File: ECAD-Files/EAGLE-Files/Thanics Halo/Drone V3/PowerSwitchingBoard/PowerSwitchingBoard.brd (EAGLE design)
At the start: 70 x 50 mm, 72 parts, among them IC1 MEGA8-AI, J1 ESC_CONTACTS, Q1 BC817, Q2 BC817, Q3 IRLR8726, Q4 IRLR8726, Q5 IRLR8726, Q6 IRLR8726, Q7 BC817, Q8 IRLR8726, Q9 IRLR8726, U1 TPS65261RHBR

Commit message: Added Flight ESCs and power supply to PowerSwitchingBoard
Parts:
- removed R12: 10k, 10k-resistor:RC0805N
- added C10, C48, C6: 470uF, 470uF-capacitor:PCAP_10X10-ELECT-M
- added C11, C27, C45: 10nF, thanics_robotics:0603_CAPACITOR
- added C12, C38, C46: 0.1uF, 0.1uF X7R Ceramic Capacitor:0805
- added C26, C44, C47, C9: 10uF, 10uF X5R Ceramic Capacitor:G-21
- added C28, C29, C30, C33, C34, C35, C39, C40, C41: 0.1uF (50V), 0.1uF-capacitor-0402:0402-M
- added C31, C36, C42, C5: 0.1uF, 0.1uF-capacitor-0402:0402-M
- added C32, C37, C43, C7: 2.2uF, 2.2uF X5R Capacitor:G-188-M
- added C8: 22uF, 22uF X5R Ceramic Capacitor:G-21
- added D10, D11, D12, D13, D14, D15, D7, D8, D9: 1N4148, 1n4148w-diode:SOD123-M
- added IC3, IC4, IC5: MEGA8-AI, atmel:TQFP32-08
- added JP3, JP4, JP5: JUMPER-SMT_2_NO_NO-SILK, SparkFun-Jumpers:SMT-JUMPER_2_NO_NO-SILK
- added Q19, Q22, Q25, Q28, Q31, Q34, Q37, Q40, Q43: BC817, SparkFun-DiscreteSemi:SOT23-3
- added Q20, Q21, Q23, Q24, Q26, Q27, Q29, Q30, Q32, Q33, Q35, Q36, Q38, Q39, Q41, Q42, Q44, Q45: IRLR8726, thanics_robotics:DPAK
- added R100, R105, R121, R127, R132, R67, R73, R78, R94: 2.2k, 2.2k-resistor:RC0603N-M
- added R101, R106, R114, R115, R116, R122, R128, R133, R141, R142, R143, R68, R74, R79, R87, R88, R89, R95: 4.7k, 4.7k-resistor:RC0603N-M
- added R102, R103, R107, R108, R124, R125, R129, R130, R134, R135, R70, R71, R75, R76, R80, R81, R97, R98: 100R, 100-resistor:RC0603N-M
- added R104, R117, R118, R119, R120, R126, R131, R144, R145, R37, R38, R65, R66, R72, R77, R90, R91, R92, R93, R99: 10k, 10k-resistor(0603):RC0603N-M
- added R109, R110, R111, R112, R113, R123, R136, R137, R138, R139, R140, R69, R82, R83, R84, R85, R86, R96: 47k, 47k-resistor:RC0603N-M
- added U2, U3: SN74LS139ADRD16-M, sn74ls139:D16-M
- added U4, U5, U6: DRV8313, DRV8313_BLDC_Driver:PWP28_5P18X3P1-M
- added U7: 74LVC1G10DW-7, 3-input-nand:SOT-363
- added U8: STM32F103RCT6LQFP-64-M, stm32f103:LQFP-64-M
- added X1, X3, X4, X5: 16MHz, thanics_robotics:3-SMD
- C19: value 10uF -> 22uF; device thanics_robotics:0805_CAPACITOR -> 22uF X5R Ceramic Capacitor:G-21
- C25: value 100uF -> 22uF; device thanics_robotics:1210_CAPACITOR -> 22uF X5R Ceramic Capacitor:G-21
- Q3: value IRLR8726 -> BC817; device thanics_robotics:DPAK -> SparkFun-DiscreteSemi:SOT23-3
- Q7: value BC817 -> IRLR8726; device SparkFun-DiscreteSemi:SOT23-3 -> thanics_robotics:DPAK
- R10, R11: device 10k-resistor:RC0805N -> 10k-resistor(0603):RC0603N-M
- R2: value 100k -> 10k; device 100k-resistor:RC0603N-M -> 10k-resistor(0603):RC0603N-M
- R9: value 158k -> 20k; device 158k-resistor:RC0402N-M -> 20k-resistor:RC0402N-M
- moved R34 267.7 mm to (33.7, 30.1)
- moved R36 267.4 mm to (29.7, 26.0)
- moved R35 267.2 mm to (29.7, 28.3)
- moved R33 264.1 mm to (29.7, 30.1), turned to 180 degrees
- moved J1 264.0 mm to (26.2, 83.3), flipped to the bottom
- moved R32 261.2 mm to (33.7, 28.3), turned to 180 degrees
- moved R31 256.7 mm to (33.7, 26.0), turned to 180 degrees
- moved R30 255.6 mm to (25.9, 30.1), turned to 180 degrees
- moved R29 251.5 mm to (25.9, 28.3), turned to 180 degrees
- moved R27 188.1 mm to (20.1, 31.5), turned to 180 degrees
- moved Q7 182.9 mm to (6.86, 36.8), flipped to the bottom, turned to 90 degrees
- moved R25 182.2 mm to (16.8, 31.5)
- moved R28 181.5 mm to (14.5, 29.0)
- moved R24 179.7 mm to (14.5, 27.2), turned to 180 degrees
- moved C4 178.6 mm to (14.0, 31.5), turned to 180 degrees
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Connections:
- removed net +10V: C25.2, L1.P$1, R12.1, R9.1
- removed net N$46: IC1.15
- removed net N$48: IC1.17
- removed net V_BATT: C13.2, C18.2, C2.2, U1.12, U1.13, U1.28, U1.29
- new net +1V8: C25.2, L1.P$1, R9.1
- new net A0: U4.27, U8.27
- new net A1: U5.27, U8.22
- new net A2: U6.27, U8.62
- new net AHIN2: IC4.27, R95.2
- new net AHIN3: IC3.27, R68.2
- new net AHIN4: IC5.27, R122.2
- new net ALIN2: IC4.30, R92.1, R98.2
- new net ALIN3: IC3.30, R65.1, R71.2
- new net ALIN4: IC5.30, R119.1, R125.2
- new net AOUT2: C33.2, Q29.3, Q30.2, R113.1
- new net AOUT3: C28.2, Q20.3, Q21.2, R86.1
- new net AOUT4: C39.2, Q38.3, Q39.2, R140.1
- new net A_SENSE2: IC4.24, R110.1, R113.2, R114.1
- new net A_SENSE3: IC3.24, R83.1, R86.2, R87.1
- new net A_SENSE4: IC5.24, R137.1, R140.2, R141.1
- new net B0: U4.25, U8.26
- new net B1: U5.25, U8.17
- new net B2: U6.25, U8.15
- new net BHIN2: IC4.31, R101.2
- new net BHIN3: IC3.31, R74.2
- new net BHIN4: IC5.31, R128.2
- new net BLIN2: IC4.28, R103.2, R99.1
- new net BLIN3: IC3.28, R72.1, R76.2
- new net BLIN4: IC5.28, R126.1, R130.2
- new net BOOT1: U8.28
- new net BOUT2: C34.2, Q32.3, Q33.2, R112.1
- new net BOUT3: C29.2, Q23.3, Q24.2, R85.1
- new net BOUT4: C40.2, Q41.3, Q42.2, R139.1
- new net B_SENSE2: IC4.23, R109.1, R112.2, R115.1
- new net B_SENSE3: IC3.23, R82.1, R85.2, R88.1
- new net B_SENSE4: IC5.23, R136.1, R139.2, R142.1
- new net C0: U4.23, U8.23
- new net C1: U5.23, U8.16
- new net C2: U6.23, U8.61
- new net CHIN2: IC4.1, R106.2
- new net CHIN3: IC3.1, R79.2
- new net CHIN4: IC5.1, R133.2
- new net CLIN2: IC4.9, R104.1, R108.2
- new net CLIN3: IC3.9, R77.1, R81.2
- new net CLIN4: IC5.9, R131.1, R135.2
- new net COUT2: C35.2, Q35.3, Q36.2, R111.1
- new net COUT3: C30.2, Q26.3, Q27.2, R84.1
- new net COUT4: C41.2, Q44.3, Q45.2, R138.1
- new net C_SENSE2: IC4.22, R111.2, R116.1, R96.1
- new net C_SENSE3: IC3.22, R69.1, R84.2, R89.1
- new net C_SENSE4: IC5.22, R123.1, R138.2, R143.1
- new net FAULT: U7.4
- new net FAULT1: U4.18, U7.1
- new net FAULT2: U5.18, U7.3
- new net FAULT3: U6.18, U7.6
- new net LIPO: U8.21
- new net MISO: U3.15
- new net MISO1: IC1.16, U3.12
- new net MISO2: IC4.16, U3.11
- new net MISO3: IC3.16, U3.10
- new net MISO4: IC5.16, U3.9
- new net MOSI: U3.1
- new net MOSI1: IC1.15, U3.4
- new net MOSI2: IC4.15, U3.5
- new net MOSI3: IC3.15, U3.6
- new net MOSI4: IC5.15, U3.7
- new net MOT0_1: U4.5
- new net MOT0_2: U4.8
- new net MOT0_3: U4.9
- new net MOT1_1: U5.5
- new net MOT1_2: U5.8
- new net MOT1_3: U5.9
- new net MOT2_1: U6.5
- new net MOT2_2: U6.8
- new net MOT2_3: U6.9
- new net N$100: IC4.7, X4.3
- new net N$101: IC4.8, X4.1
- new net N$103: Q37.1, R122.1
- new net N$104: Q38.1, R124.1
- new net N$105: Q37.3, R121.2, R124.2
- new net N$106: C39.1, D13.C, R121.1
- new net N$107: Q39.1, R125.1
- new net N$108: Q40.1, R128.1
- new net N$109: Q41.1, R129.1
- new net N$110: Q40.3, R127.2, R129.2
- new net N$111: C40.1, D14.C, R127.1
- new net N$112: Q42.1, R130.1
- new net N$113: Q43.1, R133.1
- new net N$114: Q44.1, R134.1
- new net N$115: Q43.3, R132.2, R134.2
- new net N$116: C41.1, D15.C, R132.1
- new net N$117: Q45.1, R135.1
- new net N$118: IC5.12, R144.2
- new net N$119: IC5.19, JP5.1
- new net N$120: C42.2, IC5.20
- new net N$121: IC5.7, X5.3
- new net N$122: IC5.8, X5.1
- new net N$44: IC1.12, R37.2
- new net N$61: Q19.1, R68.1
- new net N$62: Q20.1, R70.1
- new net N$63: Q19.3, R67.2, R70.2
- new net N$64: C28.1, D7.C, R67.1
- new net N$65: Q21.1, R71.1
- new net N$66: Q22.1, R74.1
- new net N$67: Q23.1, R75.1
- new net N$68: Q22.3, R73.2, R75.2
- new net N$69: C29.1, D8.C, R73.1
- new net N$70: Q24.1, R76.1
- new net N$71: Q25.1, R79.1
- new net N$72: Q26.1, R80.1
- new net N$73: Q25.3, R78.2, R80.2
- new net N$74: C30.1, D9.C, R78.1
- new net N$75: Q27.1, R81.1
- new net N$76: IC3.12, R90.2
- new net N$77: IC3.19, JP3.1
- new net N$78: C31.2, IC3.20
- new net N$79: IC3.7, X3.3
- new net N$80: IC3.8, X3.1
- new net N$82: Q28.1, R95.1
- new net N$83: Q29.1, R97.1
- new net N$84: Q28.3, R94.2, R97.2
- new net N$85: C33.1, D10.C, R94.1
- new net N$86: Q30.1, R98.1
- new net N$87: Q31.1, R101.1
- new net N$88: Q32.1, R102.1
- new net N$89: Q31.3, R100.2, R102.2
- new net N$90: C34.1, D11.C, R100.1
- new net N$91: Q33.1, R103.1
- new net N$92: Q34.1, R106.1
- new net N$93: Q35.1, R107.1
- new net N$94: Q34.3, R105.2, R107.2
- new net N$95: C35.1, D12.C, R105.1
- new net N$96: Q36.1, R108.1
- new net N$97: IC4.12, R117.2
- new net N$98: IC4.19, JP4.1
- new net N$99: C36.2, IC4.20
- new net NEUTRAL_SENSE2: IC4.10, R109.2, R110.2, R96.2
- new net NEUTRAL_SENSE3: IC3.10, R69.2, R82.2, R83.2
- new net NEUTRAL_SENSE4: IC5.10, R123.2, R136.2, R137.2
- new net PW4: R144.1, R145.1
- new net PWM: R37.1, R38.1
- new net PWM2: R117.1, R118.1
- new net PWM3: R90.1, R91.1
- new net RESET: U8.7
- new net RST: U2.1
- new net RST1: IC1.29, R3.1, U2.4
- new net RST2: IC4.29, R93.1, U2.5
- new net RST3: IC3.29, R66.1, U2.6
- new net RST4: IC5.29, R120.1, U2.7
- new net SCK: U2.15
- new net SCK1: IC1.17, U2.12
- new net SCK2: IC4.17, U2.11
- new net SCK3: IC3.17, U2.10
- new net SCK4: IC5.17, U2.9
- new net SCL: U8.29
- new net SCL2: U8.58
- new net SDA: U8.30
- new net SDA2: U8.59
- new net SEL1: U2.14, U2.2, U3.14, U3.2
- new net SEL2: U2.13, U2.3, U3.13, U3.3
- new net SWCLK: U8.49
- new net SWDIO: U8.46
- net +3V3: now also U8.1, U8.13, U8.19, U8.32, U8.48, U8.64; no longer R10.1
- net +5V: now also C32.2, C37.2, C43.2, C7.2, IC3.18, IC3.4, IC3.6, IC4.18, IC4.4, IC4.6, IC5.18, IC5.4, IC5.6, R120.2, R66.2, R93.2, U2.16, U3.16, U4.16, U4.17, U4.22, U4.24, U4.26, U5.16, U5.17, U5.22, U5.24, U5.26, U6.16, U6.17, U6.22, U6.24, U6.26, U7.5; no longer R11.1
- net AHIN: now also IC1.27
- net ALIN: now also IC1.30
- net A_SENSE: now also IC1.24
- net BHIN: now also IC1.31
- net BLIN: now also IC1.28
- net BOUT: now also Q6.3, Q7.2; no longer Q3.3, Q6.2
- net B_SENSE: now also IC1.23
- net CHIN: now also IC1.1
- net CLIN: now also IC1.9
- net C_SENSE: now also IC1.22
- net GND: now also C10.2, C26.1, C31.1, C32.1, C36.1, C37.1, C42.1, C43.1, C44.1, C47.1, C48.2, C5.1, C6.2, C7.1, C8.2, C9.2, IC3.21, IC3.3, IC3.5, IC4.21, IC4.3, IC4.5, IC5.21, IC5.3, IC5.5, JP1.2, JP3.2, JP4.2, JP5.2, Q19.2, Q21.3, Q22.2, Q24.3, Q25.2, Q27.3, Q28.2, Q3.2, Q30.3, Q31.2, Q33.3, Q34.2, Q36.3, Q37.2, Q39.3, Q40.2, Q42.3, Q43.2, Q45.3, Q7.3, R104.2, R114.2, R115.2, R116.2, R118.2, R119.2, R126.2, R131.2, R141.2, R142.2, R143.2, R145.2, R2.2, R38.2, R65.2, R72.2, R77.2, R87.2, R88.2, R89.2, R91.2, R92.2, R99.2, U2.8, U3.8, U4.10, U4.14, U4.20, U4.28, U4.29, U4.6, U4.7, U5.10, U5.14, U5.20, U5.28, U5.29, U5.6, U5.7, U6.10, U6.14, U6.20, U6.28, U6.29, U6.6, U6.7, U7.2, U8.12, U8.18, U8.31, U8.47, U8.63, X1.2, X3.2, X4.2, X5.2; no longer Q6.3, Q7.2, R12.2
- net N$1: now also C11.1, U4.2; no longer IC1.29, R3.1
- net N$10: now also Q6.1; no longer Q3.1
- net N$13: now also R2.1
- net N$17: now also R10.1
- net N$24: now also Q7.1; no longer Q6.1
- net N$25: now also Q3.1; no longer Q7.1
- net N$3: now also R11.1
- net N$31: now also Q3.3; no longer Q7.3
- net N$34: now also C5.2, IC1.20; no longer IC1.23
- net N$35: now also IC1.7, X1.3; no longer IC1.24
- net N$36: now also IC1.8, X1.1; no longer IC1.27
- net N$37: now also C11.2, U4.1; no longer IC1.28
- net N$38: now also JP1.1
- net N$39: now also C27.1, U5.2; no longer IC1.22
- net N$40: now also C27.2, U5.1; no longer IC1.30
- net N$41: now also C38.2, U5.3; no longer IC1.31
- net N$42: now also C45.1, U6.2; no longer IC1.1
- net N$43: now also C45.2, U6.1; no longer IC1.9
- net N$45: now also C46.2, U6.3; no longer IC1.12
- net N$47: now also C12.2, U4.3; no longer IC1.16
- net VDD: now also C10.1, C12.1, C13.2, C18.2, C2.2, C26.2, C38.1, C44.2, C46.1, C47.2, C48.1, C6.1, C8.1, C9.1, D10.A, D11.A, D12.A, D13.A, D14.A, D15.A, D7.A, D8.A, D9.A, Q20.2, Q23.2, Q26.2, Q29.2, Q32.2, Q35.2, Q38.2, Q41.2, Q44.2, Q6.2, U1.12, U1.13, U1.28, U1.29, U4.11, U4.4, U5.11, U5.4, U6.11, U6.4; no longer Q3.2
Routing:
- net +5V: track 0.00 -> 60.6 mm
- net AOUT3: track 0.00 -> 51.0 mm, vias 0 -> 17
- net AOUT2: track 0.00 -> 49.5 mm, vias 0 -> 17
- net AOUT: track 0.00 -> 47.4 mm, vias 0 -> 17
- net VDD: track 0.00 -> 47.1 mm, vias 0 -> 8
- net AOUT4: track 0.00 -> 46.7 mm, vias 0 -> 17
- net BOUT3: track 0.00 -> 33.7 mm, vias 0 -> 18
- net BOUT: track 0.00 -> 33.5 mm, vias 0 -> 16
- net BOUT4: track 0.00 -> 33.5 mm, vias 0 -> 18
- net BOUT2: track 0.00 -> 33.5 mm, vias 0 -> 18
- net BLIN2: track 0.00 -> 32.4 mm, vias 0 -> 2
- net BLIN4: track 0.00 -> 32.4 mm, vias 0 -> 2
- net BLIN3: track 0.00 -> 32.4 mm, vias 0 -> 2
- net BLIN: track 0.00 -> 32.3 mm, vias 0 -> 2
- net CLIN: track 0.00 -> 27.9 mm, vias 0 -> 2
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- added copper zone on layer 1, net AOUT
- added copper zone on layer 16, net AOUT
- added copper zone on layer 1, net AOUT2
- added copper zone on layer 16, net AOUT2
- added copper zone on layer 1, net AOUT3
- added copper zone on layer 16, net AOUT3
- added copper zone on layer 1, net AOUT4
- added copper zone on layer 16, net AOUT4
- added copper zone on layer 1, net BOUT
- added copper zone on layer 16, net BOUT
- added copper zone on layer 1, net BOUT2
- added copper zone on layer 16, net BOUT2
- added copper zone on layer 1, net BOUT3
- added copper zone on layer 16, net BOUT3
- added copper zone on layer 1, net BOUT4
- added copper zone on layer 16, net BOUT4
- added copper zone on layer 1, net COUT
- added copper zone on layer 16, net COUT
- added copper zone on layer 1, net COUT2
- added copper zone on layer 16, net COUT2
- added copper zone on layer 1, net COUT3
- added copper zone on layer 16, net COUT3
- added copper zone on layer 1, net COUT4
- added copper zone on layer 16, net COUT4
- added copper zone on layer 1, net GND
- added copper zone on layer 16, net GND
- added copper zone on layer 16, net VDD
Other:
- board size 70 x 50 mm -> 80 x 88 mm

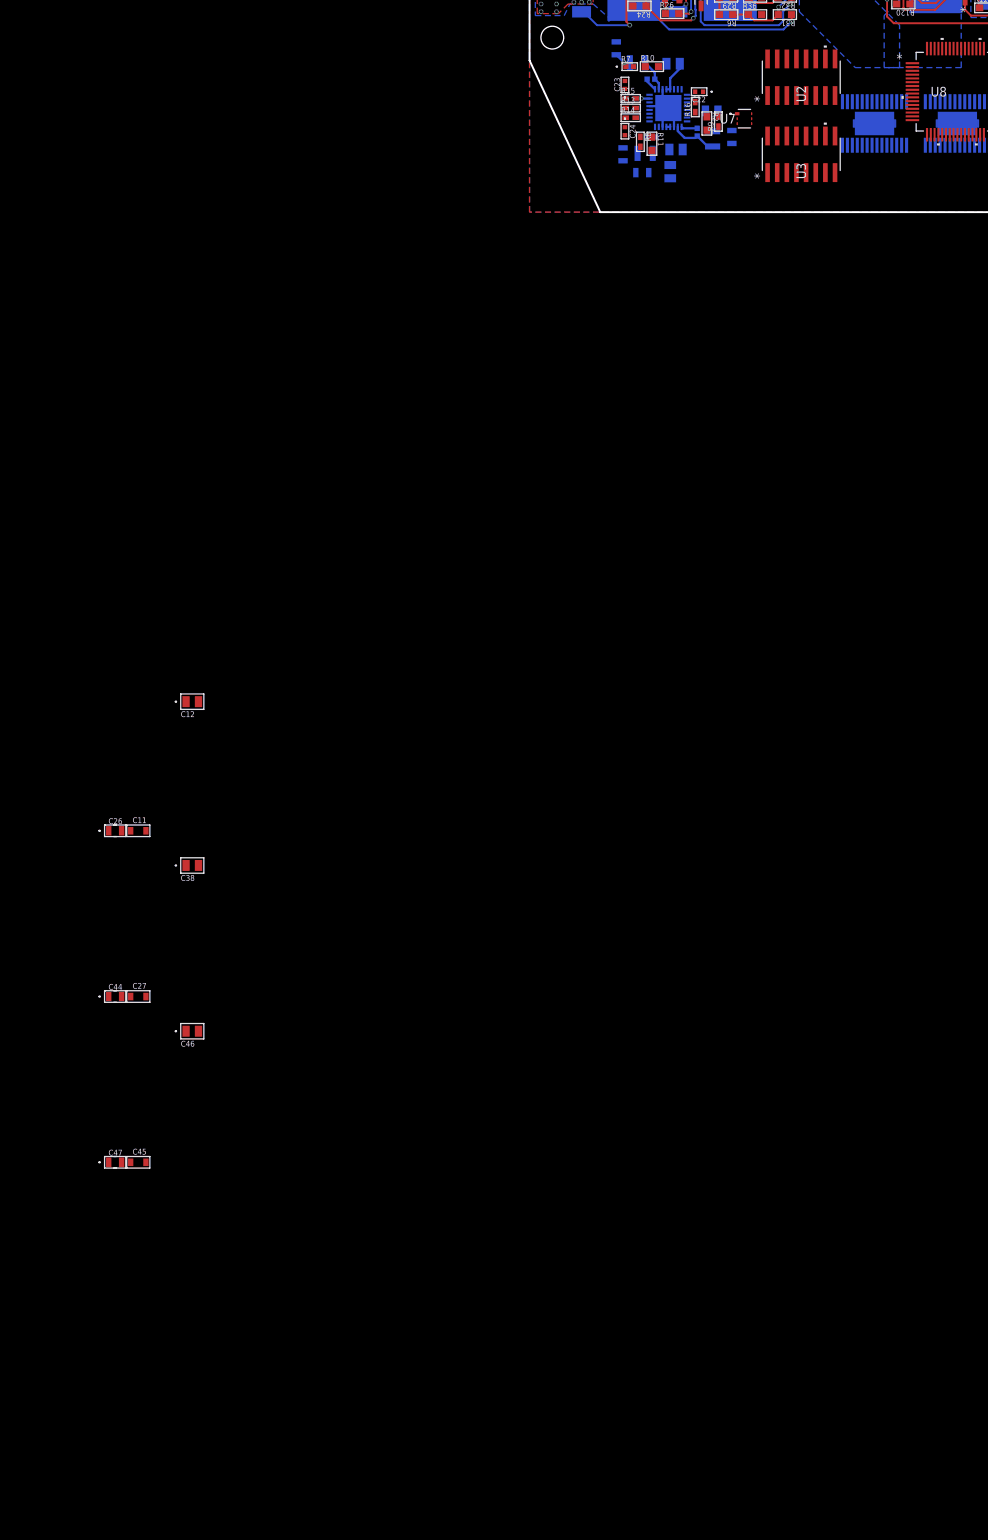
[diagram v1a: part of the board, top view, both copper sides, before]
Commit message: Added connectors
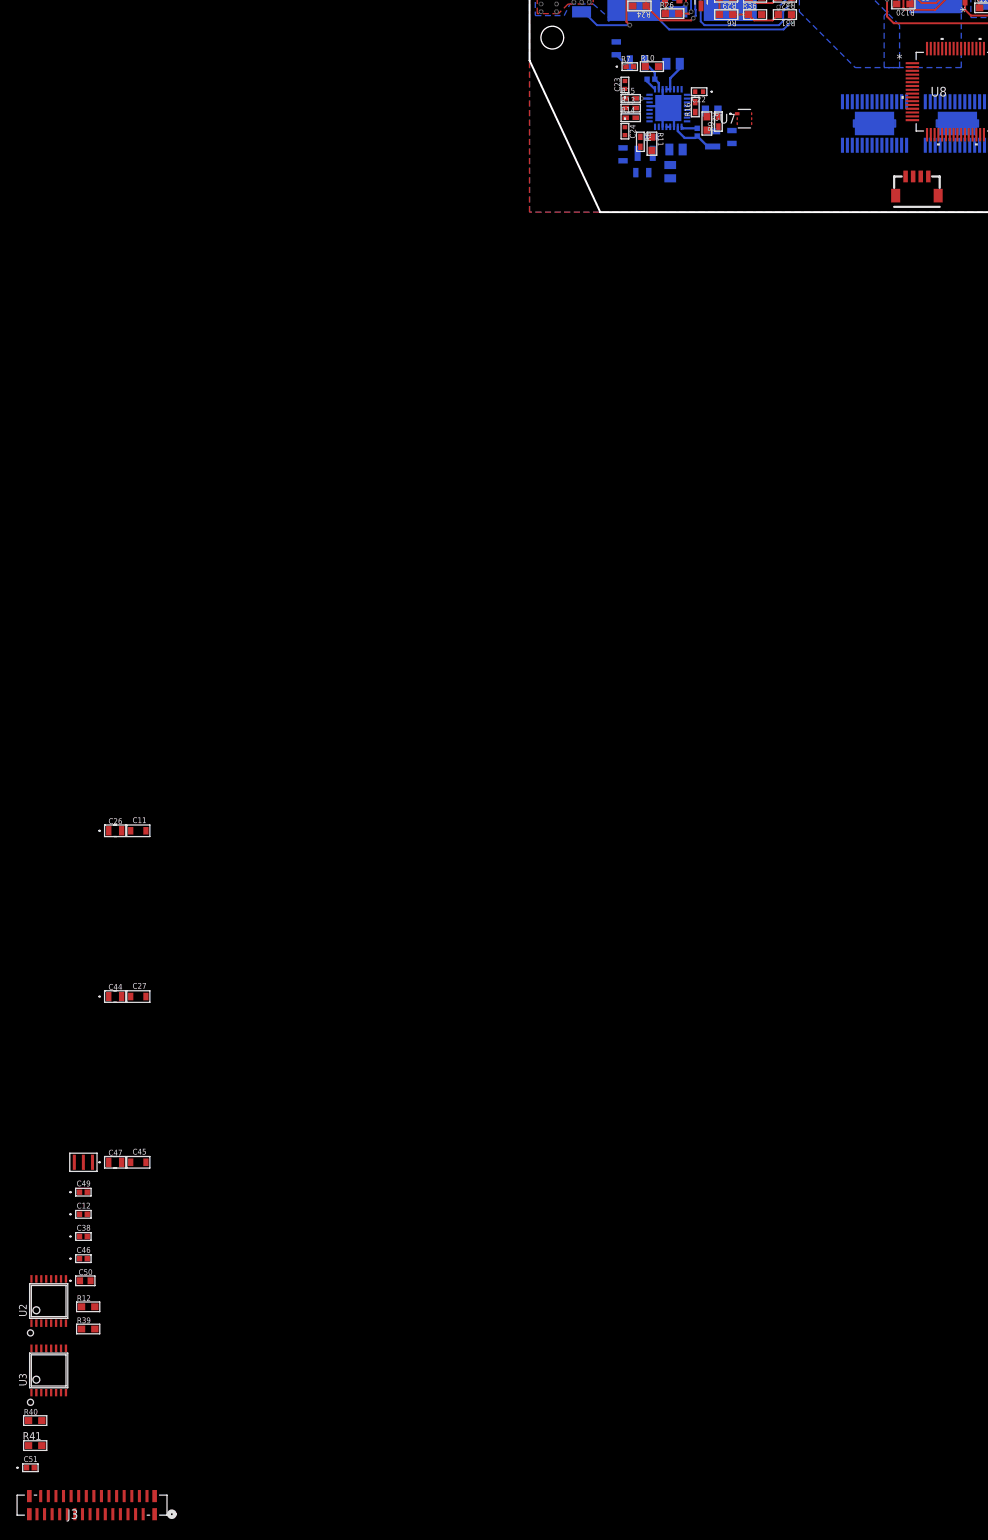
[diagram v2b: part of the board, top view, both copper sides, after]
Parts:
- added C49, C51: 0.1uF, 0.1uF-capacitor-0402:0402-M
- added C50: 2.2uF, 2.2uF X5R Capacitor:G-188-M
- added J2: (no value), thanics_robotics:JST_SH_4POS
- added J3: 62674-301121ALF, 30pin_ffc_connector:CON30_1X30_DUT_58XF
- added R12, R39, R40: 10k, 10k-resistor(0603):RC0603N-M
- added R41: 1.5k, 1.5k-resistor:RC0603N-M
- added X6: 8MHz, thanics_robotics:3-SMD
- C12, C38, C46: device 0.1uF X7R Ceramic Capacitor:0805 -> 0.1uF-capacitor-0402:0402-M
- U2, U3: value SN74LS139ADRD16-M -> 74HC4052PW; device sn74ls139:D16-M -> thanics_robotics:TSSOP16
- moved U2 189.3 mm to (-63.4, -143.5), turned to 0 degrees
- moved U3 188.5 mm to (-63.4, -152.7), turned to 0 degrees
- moved C12 69.1 mm to (-58.8, -132.1)
- moved C38 51.0 mm to (-58.8, -135.0)
- moved C46 33.2 mm to (-58.8, -137.9)
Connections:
- removed net SEL2: U2.13, U2.3, U3.13, U3.3
- new net BATT_SCL: J3.20
- new net BATT_SDA: J3.19
- new net BOOT0: J3.18, R12.2, U8.60
- new net N$46: U8.5, X6.3
- new net N$48: U8.6, X6.1
- new net NT-RX: J2.2, U8.52
- new net NT-TX: J2.3, U8.51
- new net RX: J3.22
- new net SEL0: J3.9, U2.10, U3.10
- new net TX: J3.21
- net +1V8: now also J3.7, J3.8
- net +3V3: now also C46.2, C50.2, J3.3, J3.4, J3.5, J3.6
- net +5V: now also J2.4, J3.1, J3.2
- net BOOT1: now also R39.2
- net GND: now also C46.1, C50.1, C51.1, J2.1, J3.23, J3.24, J3.25, J3.26, J3.27, J3.28, J3.29, J3.30, R12.1, R39.1, R41.2, U2.6, U2.7, U3.6, U3.7, X6.2
- net LIPO: now also C51.2, R40.2, R41.1
- net MISO: now also J3.13, U3.3; no longer U3.15
- net MISO1: now also U3.1; no longer U3.12
- net MISO2: now also U3.5; no longer U3.11
- net MISO3: now also U3.2; no longer U3.10
- net MISO4: now also U3.4; no longer U3.9
- net MOSI: now also J3.12, U3.13; no longer U3.1
- net MOSI1: now also U3.12; no longer U3.4
- net MOSI2: now also U3.14; no longer U3.5
- net MOSI3: now also U3.15; no longer U3.6
- net MOSI4: now also U3.11; no longer U3.7
- net N$41: now also C49.2; no longer C38.2
- net N$45: now also C38.2; no longer C46.2
- net RESET: now also J3.17
- net RST: now also J3.11, U2.13; no longer U2.1
- net RST1: now also U2.12; no longer U2.4
- net RST2: now also U2.14; no longer U2.5
- net RST3: now also U2.15; no longer U2.6
- net RST4: now also U2.11; no longer U2.7
- net SCK: now also J3.14, U2.3; no longer U2.15
- net SCK1: now also U2.1; no longer U2.12
- net SCK2: now also U2.5; no longer U2.11
- net SCK3: now also U2.2; no longer U2.10
- net SCK4: now also U2.4; no longer U2.9
- net SEL1: now also J3.10, U2.9, U3.9; no longer U2.14, U2.2, U3.14, U3.2
- net SWCLK: now also J3.16
- net SWDIO: now also J3.15
- net VDD: now also C49.1, R40.1; no longer C46.1

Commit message: Fixed consistancy errors and finished routing
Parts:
- removed D13, D14, D15: 1N4148, 1n4148w-diode:SOD123-M
- removed IC1: MEGA8-AI, atmel:TQFP32-08
- removed R39: 10k, 10k-resistor(0603):RC0603N-M
- added D4, D5, D6: 1N4148, 1n4148w-diode:SOD123-M
- added GND, SCL, SDA: TPTP20SQ, testpad:TP20SQ
- added J4, J5, J6: B3B-ZR-SM4, jst:B3B-ZR-SM4
- Q1, Q19, Q2, Q22, Q25, Q28, Q3, Q31, Q34, Q37, Q40, Q43: value BC817 -> 500mA/300V
- U7: value 74LVC1G10DW-7 -> STM32F103RCT6LQFP-64-M; device 3-input-nand:SOT-363 -> stm32f103:LQFP-64-M
- U8: value STM32F103RCT6LQFP-64-M -> MEGA8-AI; device stm32f103:LQFP-64-M -> atmel:TQFP32-08
- moved C51 206.7 mm to (51.1, 5.08), flipped to the bottom, turned to 270 degrees
- moved R41 204.4 mm to (52.6, 4.57), flipped to the bottom, turned to 270 degrees
- moved R12 200.6 mm to (56.3, 20.4), flipped to the bottom
- moved R40 199.4 mm to (50.0, 3.56), flipped to the bottom, turned to 180 degrees
- moved J3 195.1 mm to (30.2, 3.68), turned to 180 degrees
- moved C50 194.3 mm to (62.5, 11.2), turned to 180 degrees
- moved C46 194.1 mm to (50.2, 22.7)
- moved U3 192.6 mm to (35.2, 12.8), turned to 270 degrees
- moved U2 190.4 mm to (35.2, 19.4), turned to 270 degrees
- moved C12 190.2 mm to (70.4, 7.49), flipped to the bottom, turned to 180 degrees
- moved C49 180.3 mm to (58.8, 7.49), flipped to the bottom, turned to 180 degrees
- moved X6 179.5 mm to (48.3, 18.8), turned to 270 degrees
- moved C38 177.1 mm to (48.3, 6.10), flipped to the bottom, turned to 180 degrees
- moved C45 167.2 mm to (49.3, 8.13), flipped to the bottom, turned to 90 degrees
- moved C47 164.6 mm to (41.5, 8.38), flipped to the bottom, turned to 90 degrees
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- renumbered IC3 to U10, IC4 to U9, IC5 to U11
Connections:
- removed net BOOT1: R39.2, U8.28
- removed net PW4: R144.1, R145.1
- new net PWM4: J3.26, R144.1, R145.1
- net +3V3: now also U7.1, U7.13, U7.19, U7.32, U7.48, U7.64; no longer U8.1, U8.13, U8.19, U8.32, U8.48, U8.64
- net +5V: now also U8.18, U8.4, U8.6; no longer IC1.18, IC1.4, IC1.6, U7.5
- net A0: now also U7.27; no longer U8.27
- net A1: now also U7.22; no longer U8.22
- net A2: now also U7.62; no longer U8.62
- net AHIN: now also U8.27; no longer IC1.27
- net ALIN: now also U8.30; no longer IC1.30
- net A_SENSE: now also U8.24; no longer IC1.24
- net B0: now also U7.26; no longer U8.26
- net B1: now also U7.17; no longer U8.17
- net B2: now also U7.15; no longer U8.15
- net BATT_SCL: now also SCL.TP
- net BATT_SDA: now also SDA.TP
- net BHIN: now also U8.31; no longer IC1.31
- net BLIN: now also U8.28; no longer IC1.28
- net BOOT0: now also U7.60; no longer U8.60
- net B_SENSE: now also U8.23; no longer IC1.23
- net C0: now also U7.23; no longer U8.23
- net C1: now also U7.16; no longer U8.16
- net C2: now also U7.61; no longer U8.61
- net CHIN: now also U8.1; no longer IC1.1
- net CLIN: now also U8.9; no longer IC1.9
- net C_SENSE: now also U8.22; no longer IC1.22
- net FAULT: now also J3.27; no longer U7.4
- net FAULT1: no longer U7.1
- net FAULT2: no longer U7.3
- net FAULT3: no longer U7.6
- net GND: now also GND.TP, U7.12, U7.18, U7.28, U7.31, U7.47, U7.63, U8.21, U8.3, U8.5; no longer IC1.21, IC1.3, IC1.5, J3.23, J3.24, J3.25, J3.26, J3.27, R39.1, U7.2, U8.12, U8.18, U8.31, U8.47, U8.63
- net LIPO: now also U7.21; no longer U8.21
- net MISO1: now also U8.16; no longer IC1.16
- net MOSI1: now also U8.15; no longer IC1.15
- net MOT0_1: now also J4.1
- net MOT0_2: now also J4.2
- net MOT0_3: now also J4.3
- net MOT1_1: now also J5.1
- net MOT1_2: now also J5.2
- net MOT1_3: now also J5.3
- net MOT2_1: now also J6.1
- net MOT2_2: now also J6.2
- net MOT2_3: now also J6.3
- net N$106: now also D10.C; no longer D13.C
- net N$111: now also D11.C; no longer D14.C
- net N$116: now also D12.C; no longer D15.C
- net N$34: now also U8.20; no longer IC1.20
- net N$35: now also U8.7; no longer IC1.7
- net N$36: now also U8.8; no longer IC1.8
- net N$38: now also U8.19; no longer IC1.19
- net N$44: now also U8.12; no longer IC1.12
- net N$46: now also U7.5; no longer U8.5
- net N$48: now also U7.6; no longer U8.6
- net N$85: now also D4.C; no longer D10.C
- net N$90: now also D5.C; no longer D11.C
- net N$95: now also D6.C; no longer D12.C
- net NEUTRAL_SENSE: now also U8.10; no longer IC1.10
- net NT-RX: now also U7.52; no longer U8.52
- net NT-TX: now also U7.51; no longer U8.51
- net PWM: now also J3.23
- net PWM2: now also J3.24
- net PWM3: now also J3.25
- net RESET: now also U7.7; no longer U8.7
- net RST1: now also U8.29; no longer IC1.29
- net RX: now also U7.43
- net SCK1: now also U8.17; no longer IC1.17
- net SCL: now also U7.29; no longer U8.29
- net SCL2: now also U7.58; no longer U8.58
- net SDA: now also U7.30; no longer U8.30
- net SDA2: now also U7.59; no longer U8.59
- net SWCLK: now also U7.49; no longer U8.49
- net SWDIO: now also U7.46; no longer U8.46
- net TX: now also U7.42
- net VDD: now also D4.A, D5.A, D6.A; no longer D13.A, D14.A, D15.A
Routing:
- net +5V: track 60.6 -> 310.5 mm, vias 0 -> 21
- net VDD: track 47.1 -> 196.0 mm, vias 8 -> 23
- net +3V3: track 2.83 -> 123.4 mm, vias 1 -> 6
- net BATT_SDA: track 0.00 -> 113.4 mm, vias 0 -> 3
- net BATT_SCL: track 0.00 -> 109.5 mm, vias 0 -> 3
- net PWM3: track 1.78 -> 78.7 mm
- net RST3: track 2.18 -> 72.7 mm, vias 0 -> 4
- net MISO3: track 0.00 -> 69.1 mm, vias 0 -> 2
- net MOSI3: track 0.00 -> 64.7 mm, vias 0 -> 2
- net MISO2: track 0.00 -> 61.7 mm, vias 0 -> 2
- net RST2: track 2.18 -> 63.4 mm, vias 0 -> 4
- net SCK3: track 0.00 -> 60.7 mm, vias 0 -> 2
- net PWM2: track 1.78 -> 61.4 mm, vias 0 -> 2
- net MOSI2: track 0.00 -> 56.3 mm
- net SCK2: track 0.00 -> 55.8 mm, vias 0 -> 2
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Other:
- board text added: "*Made on Earth by humans*"
- board text added: "ESC1"
- board text added: "ESC2"
- board text added: "ESC3"
- board text added: "ESC4"
- board text added: "MOT0"
- board text added: "MOT1"
- board text added: "MOT2"
- board text added: "Power Switching Board v1"
- board text added: "To Batt ->"
- board text added: "To FC ->"
- board text added: "To Gimbal ->"

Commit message: Finished Power Switching Board and Flight Controller Board v1
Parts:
- moved C43 2.81 mm to (45.5, 34.8), turned to 90 degrees
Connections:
- removed net FAULT: J3.27
- net GND: now also J3.27
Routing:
- net +5V: track 310.5 -> 307.2 mm
- net RST3: track 72.7 -> 70.7 mm
- net SEL1: track 23.1 -> 24.2 mm, vias 6 -> 5
- net PWM4: track 43.7 -> 43.0 mm
- net GND: vias 221 -> 237
